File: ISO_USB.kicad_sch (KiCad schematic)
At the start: 18 parts, among them J2 USB_C_Receptacle, SW3 SW_SPST

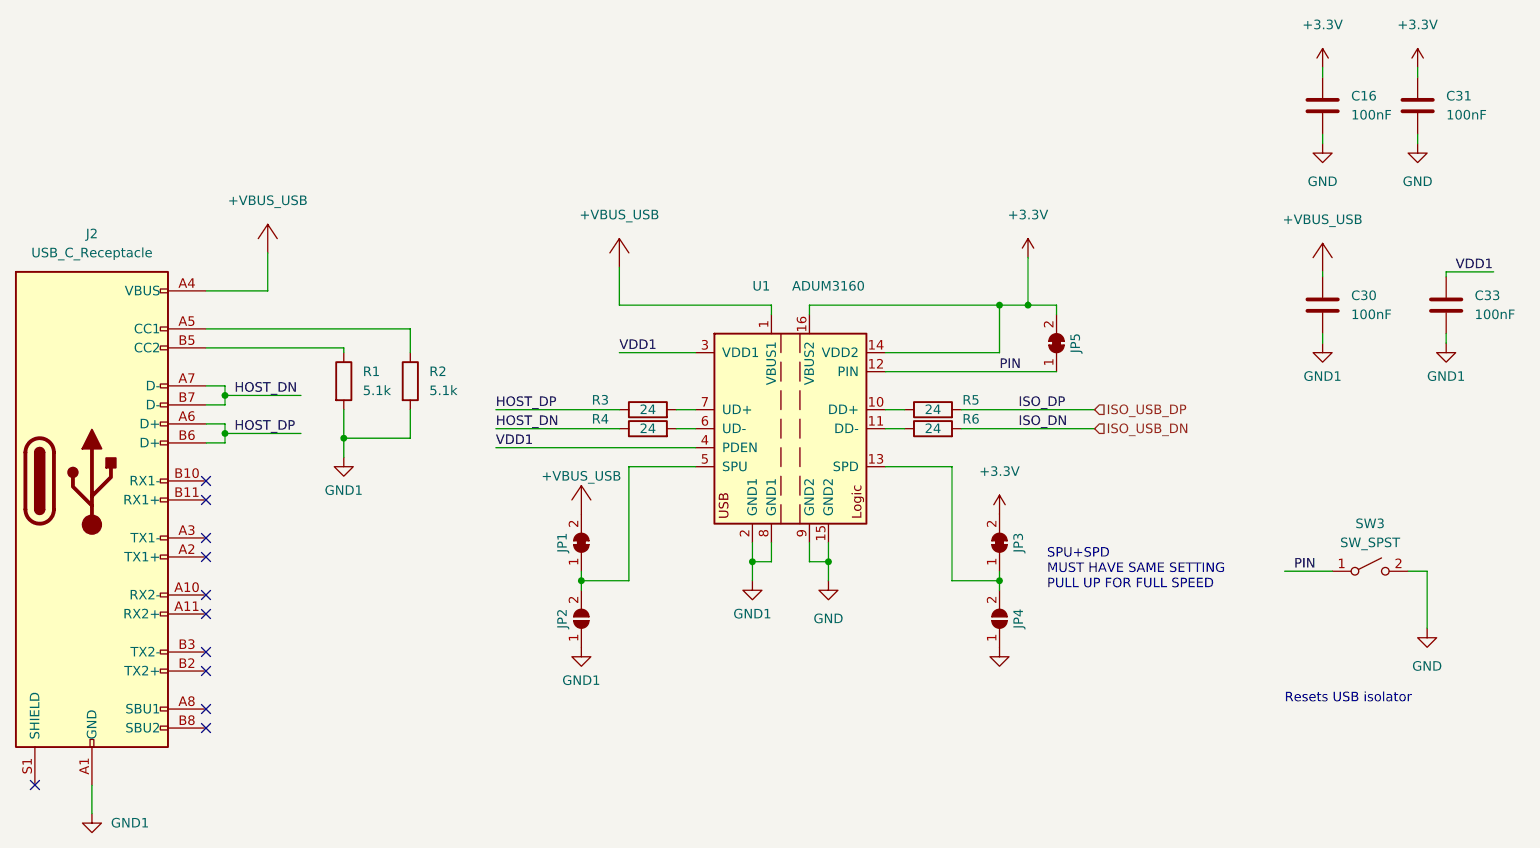
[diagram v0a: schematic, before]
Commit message: finished routing, sending to fab
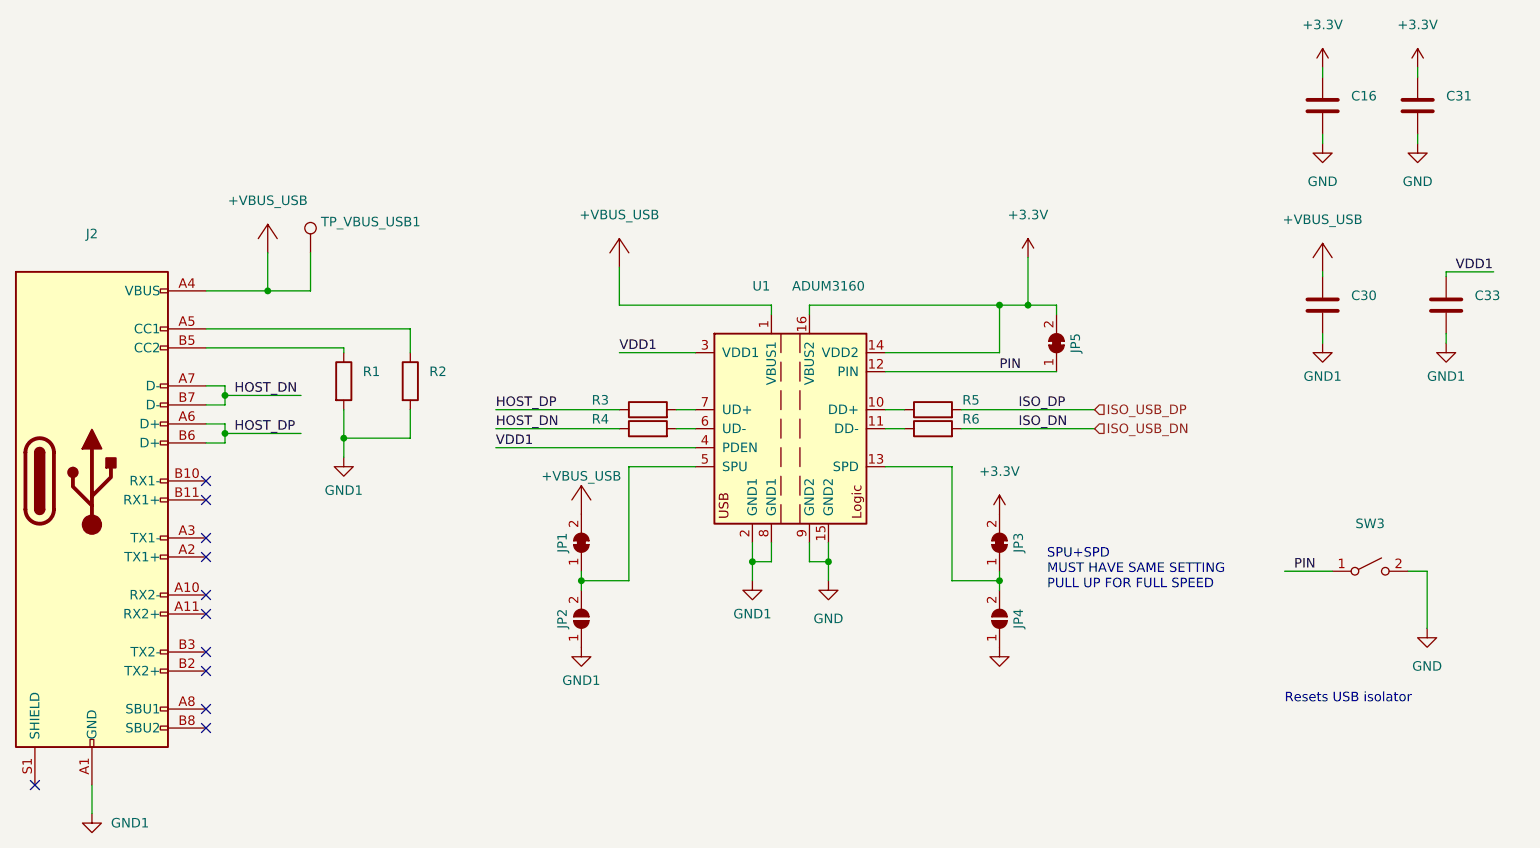
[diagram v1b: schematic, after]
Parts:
- added TP_VBUS_USB1: (no value), symbol Connector:TestPoint
- C16, C30, C31, C33: value 100nF -> (none); footprint Capacitor_SMD:C_0603_1608Metric -> (none)
- J2: value USB_C_Receptacle -> (none); footprint Connector_USB:USB_C_Receptacle_JAE_DX07S016JA1R1500 -> (none)
- JP1, JP5: value ~ -> (none); footprint Jumper:SolderJumper-2_P1.3mm_Bridged_RoundedPad1.0x1.5mm -> (none)
- JP2, JP3, JP4: value ~ -> (none); footprint Jumper:SolderJumper-2_P1.3mm_Open_RoundedPad1.0x1.5mm -> (none)
- R1, R2: value 5.1k -> (none); footprint Resistor_SMD:R_0603_1608Metric -> (none)
- R3, R4, R5, R6: value 24 -> (none); footprint Resistor_SMD:R_0603_1608Metric -> (none)
- SW3: value SW_SPST -> (none); footprint Button_Switch_SMD:SW_SPST_PTS645 -> (none)
- U1: value ~ -> (none); footprint Package_SO:SOIC-16W_7.5x10.3mm_P1.27mm -> (none)
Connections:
- net +VBUS_USB: now also TP_VBUS_USB1.1
